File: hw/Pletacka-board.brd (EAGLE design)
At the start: 4 parts

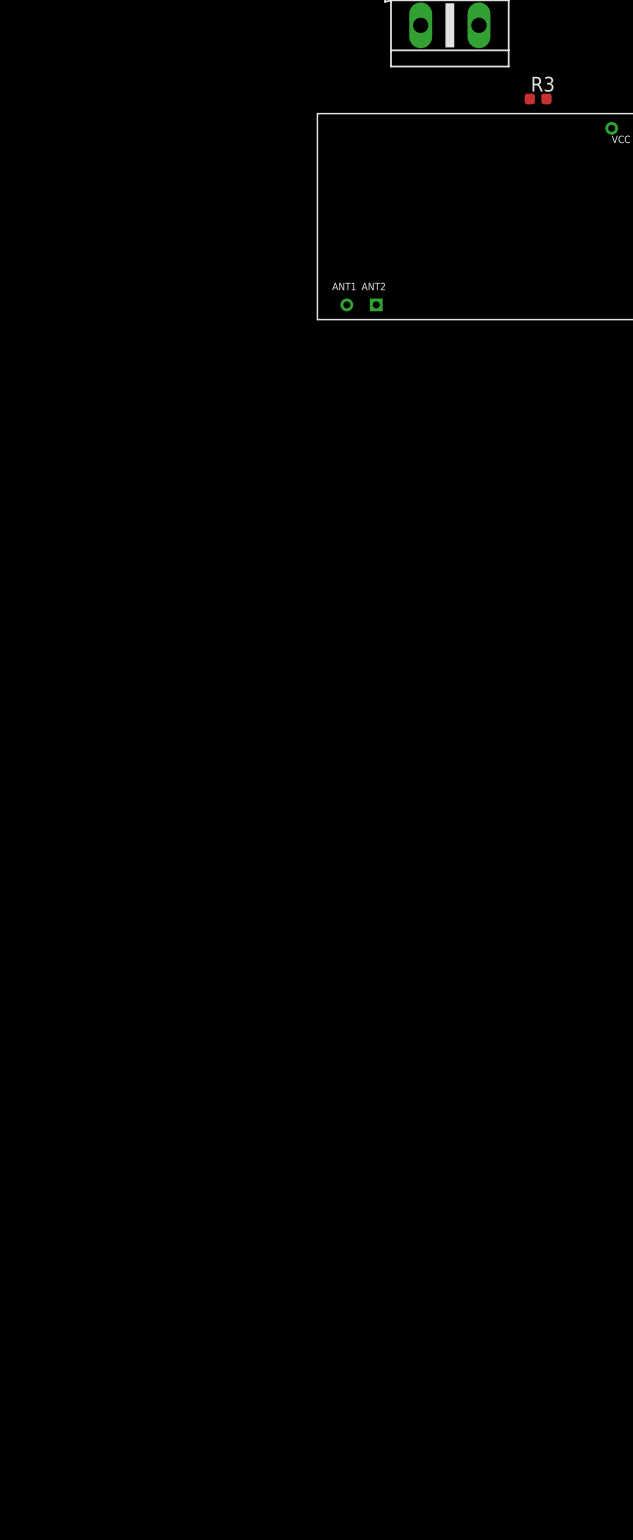
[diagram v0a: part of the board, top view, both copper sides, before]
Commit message: Add buttons and LEDs
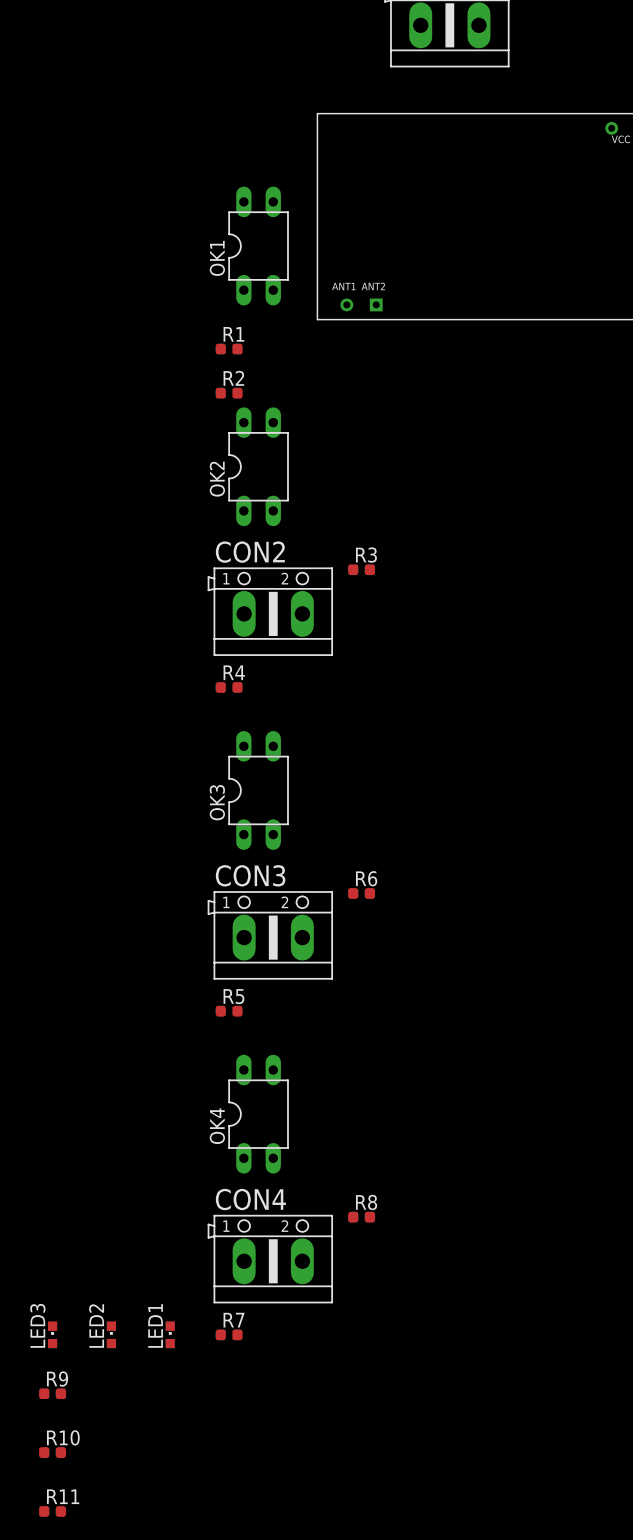
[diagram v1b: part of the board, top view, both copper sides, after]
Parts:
- added CON2, CON3, CON4: (no value), #Svorkovnice:AK500/2
- added LED1, LED2, LED3: (no value), led:CHIPLED_0603
- added OK1, OK2, OK3, OK4: PC817, #Optocleny:DIL04
- added R1, R5, R7: 1K, rcl_upravena:R0603
- added R10, R11, R9: 330R, rcl_upravena:R0603
- added R2, R4, R6, R8: 4K7, rcl_upravena:R0603
- R3: value (none) -> 1K
- moved R3 43.4 mm to (-97.8, -62.2)
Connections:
- net GPIO12 renamed BUTTON1
- removed net GPIO17: U$1.17
- removed net GPIO21: U$1.21
- removed net GPIO22: U$1.22
- removed net GPIO32: U$1.32
- removed net GPIO36: U$1.36
- removed net GPIO37: U$1.37
- removed net GPIO38: U$1.38
- removed net GPIO39: U$1.39
- new net LED_POWER: R9.2, U$1.21
- new net LED_SEND: R11.2, U$1.17
- new net LED_WIFI: R10.2, U$1.22
- new net N$1: OK1.1, R1.1
- new net N$10: CON4.2, OK4.2
- new net N$11: OK4.1, R7.1
- new net N$12: CON4.1, R7.2
- new net N$13: LED1.A, R9.1
- new net N$14: LED2.A, R10.1
- new net N$15: LED3.A, R11.1
- new net N$2: CON1.2, OK1.2
- new net N$3: CON2.2, OK2.2
- new net N$4: CON1.1, R1.2
- new net N$5: OK2.1, R3.1
- new net N$6: CON2.1, R3.2
- new net N$7: CON3.2, OK3.2
- new net N$8: OK3.1, R5.1
- new net N$9: CON3.1, R5.2
- new net OPTO1: OK1.4, R2.2, U$1.36
- new net OPTO2: OK2.4, R4.2, U$1.37
- new net OPTO3: OK3.4, R6.2, U$1.38
- new net OPTO4: OK4.4, R8.2, U$1.39
- new net RFID: RDM1.RX, U$1.32
- net +3V3: now also R2.1, R4.1, R6.1, R8.1
- net +5V: now also RDM1.VCC
- net GND: now also LED1.C, LED2.C, LED3.C, OK1.3, OK2.3, OK3.3, OK4.3, RDM1.GND

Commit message: Start routing
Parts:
- moved LED1 176.8 mm to (40.6, -43.2)
- moved LED2 176.8 mm to (35.6, -43.2)
- moved LED3 176.8 mm to (30.5, -43.2)
- moved R10 176.8 mm to (30.5, -53.3)
- moved R11 176.8 mm to (30.5, -58.4)
- moved R4 176.8 mm to (45.7, 12.7)
- moved R5 176.8 mm to (45.7, -15.2)
- moved R6 176.8 mm to (57.1, -5.08)
- moved R8 176.8 mm to (57.1, -33.0)
- moved R9 176.8 mm to (30.5, -48.3)
- moved R7 150.0 mm to (-5.08, -20.3), turned to 270 degrees
- moved OK4 143.0 mm to (0.00, -14.0)
- moved R2 141.8 mm to (26.7, -6.35), turned to 270 degrees
- moved CON4 139.3 mm to (-2.54, -27.9)
- moved OK1 138.7 mm to (30.5, -14.0)
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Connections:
- removed net N$10: CON4.2, OK4.2
- removed net N$2: CON1.2, OK1.2
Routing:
- net N$3: track 0.00 -> 10.7 mm
- net N$4: track 0.00 -> 6.15 mm
- net N$1: track 0.00 -> 4.14 mm
